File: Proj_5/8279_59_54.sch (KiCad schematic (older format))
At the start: 29 parts, among them SW10 Switch_SW_SPST, SW11 Switch_SW_SPST, SW12 Switch_SW_SPST, SW13 Switch_SW_SPST, SW14 Switch_SW_SPST, SW15 Switch_SW_SPST, SW16 Switch_SW_SPST, SW17 Switch_SW_SPST, SW18 Switch_SW_SPST, SW19 Switch_SW_SPST, SW2 Switch_SW_SPST, SW20 Switch_SW_SPST, SW21 Switch_SW_SPST, SW22 Switch_SW_SPST, SW23 Switch_SW_SPST, SW3 Switch_SW_SPST, SW4 Switch_SW_SPST, SW5 Switch_SW_SPST, SW6 Switch_SW_SPST, SW7 Switch_SW_SPST, SW8 Switch_SW_SPST, SW9 Switch_SW_SPST, U17 pkd8279, U18 74LS138

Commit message: Dont be wonky:
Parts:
- gave numbers to parts that had none: 5
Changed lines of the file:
@@
 P 6550 3000
 AR Path="/5EA98353/5EA655BD" Ref="C?"  Part="1"
-AR Path="/5EA993EC/5EA655BD" Ref="C?"  Part="1"
-F 0 "C?" V 6298 3000 50  0000 C CNN
+AR Path="/5EA993EC/5EA655BD" Ref="C11"  Part="1"
+F 0 "C11" V 6298 3000 50  0000 C CNN
 F 1 "0.1uF" V 6389 3000 50  0000 C CNN
 F 2 "" H 6588 2850 50  0001 C CNN
@@
 P 18350 4100
 AR Path="/5EA99146/5EA19E00" Ref="U?"  Part="1"
-AR Path="/5EA993EC/5EA19E00" Ref="U?"  Part="1"
-F 0 "U?" H 18350 5281 50  0000 C CNN
+AR Path="/5EA993EC/5EA19E00" Ref="U11"  Part="1"
+F 0 "U11" H 18350 5281 50  0000 C CNN
 F 1 "8254" H 18350 5190 50  0000 C CNN
 F 2 "Package_DIP:DIP-24_W15.24mm" H 18400 4350 50  0001 C CNN
@@
 AR Path="/5EA98353/5EA19E06" Ref="C?"  Part="1"
 AR Path="/5EA99146/5EA19E06" Ref="C?"  Part="1"
-AR Path="/5EA993EC/5EA19E06" Ref="C?"  Part="1"
-F 0 "C?" V 18448 2650 50  0000 C CNN
+AR Path="/5EA993EC/5EA19E06" Ref="C13"  Part="1"
+F 0 "C13" V 18448 2650 50  0000 C CNN
 F 1 "0.1uF" V 18539 2650 50  0000 C CNN
 F 2 "" H 18738 2500 50  0001 C CNN
@@
 P 13850 9850
 AR Path="/5EA99014/5EA1D8D0" Ref="U?"  Part="1"
-AR Path="/5EA993EC/5EA1D8D0" Ref="U?"  Part="1"
-F 0 "U?" H 13850 11131 50  0000 C CNN
+AR Path="/5EA993EC/5EA1D8D0" Ref="U10"  Part="1"
+F 0 "U10" H 13850 11131 50  0000 C CNN
 F 1 "8259" H 13850 11040 50  0000 C CNN
 F 2 "Package_DIP:DIP-28_W15.24mm" H 13850 9850 50  0001 C CIN
@@
 AR Path="/5EA98353/5EA1D8D6" Ref="C?"  Part="1"
 AR Path="/5EA99014/5EA1D8D6" Ref="C?"  Part="1"
-AR Path="/5EA993EC/5EA1D8D6" Ref="C?"  Part="1"
-F 0 "C?" V 13998 8500 50  0000 C CNN
+AR Path="/5EA993EC/5EA1D8D6" Ref="C12"  Part="1"
+F 0 "C12" V 13998 8500 50  0000 C CNN
 F 1 "0.1uF" V 14089 8500 50  0000 C CNN
 F 2 "" H 14288 8350 50  0001 C CNN

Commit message: Mostly finished 8279
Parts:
- removed C11: 0.1uF, symbol Device:C
- added C? (x4): 0.1uF, symbol Device:C
- added R?: R, symbol Device:R
- added SW? (x3): Switch_SW_SPST, symbol Proj_5-rescue:Switch_SW_SPST-Proj_5_Custom_LED
- added U? (x3): MAX6816, Package_TO_SOT_SMD:SOT-143, symbol Interface:MAX6816
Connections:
- net labels added: D0, D1, D2, D3, D4, D5, D6, D7, MAIN_CLK, NMI, RESET, ~RD, ~WR
- wire segments 110 -> 184
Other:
- note added: "Needs VCC Pins, Headers, Decoding"
- moved on the sheet: C12, C13

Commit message: Quick Edit to 79 Wires
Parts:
- R?: value R -> 1kOhm
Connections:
- wire segments 184 -> 187
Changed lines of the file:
@@
 	5550 5050 4700 5050
-Wire Wire Line
-	4700 550  14100 550
 Wire Wire Line
 	7150 8100 7700 8100
@@
 Wire Wire Line
 	10900 600  10900 1800
-Wire Wire Line
-	14100 600  14100 1850
 Wire Wire Line
 	4700 550  4700 5050
@@
 P 10550 8000
 F 0 "R?" H 10620 8046 50  0000 L CNN
-F 1 "R" H 10620 7955 50  0000 L CNN
+F 1 "1kOhm" H 10620 7955 50  0000 L CNN
 F 2 "" V 10480 8000 50  0001 C CNN
 F 3 "~" H 10550 8000 50  0001 C CNN
@@
 Text Notes 12550 7100 0    197  ~ 0
 Needs VCC Pins, Headers, Decoding
+Wire Wire Line
+	14100 600  14100 900
+Wire Wire Line
+	4700 550  13850 550
+Wire Wire Line
+	13850 550  13850 900
+Wire Wire Line
+	13850 900  14100 900
+Connection ~ 14100 900
+Wire Wire Line
+	14100 900  14100 1850
 $EndSCHEMATC

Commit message: Made the rest of the connections for the SRAM. Changed stuff on the main page
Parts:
- U10: symbol Interface:8259 -> Proj_5-rescue:8259-Interface
- U11: symbol Timer:8254 -> Proj_5-rescue:8254-Timer
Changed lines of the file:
@@
 	12050 3650 13050 3650
 $Comp
-L Timer:8254 U?
+L Proj_5-rescue:8254-Timer U?
 U 1 1 5EA19E00
 P 6550 7500
@@
 $EndComp
 $Comp
-L Interface:8259 U?
+L Proj_5-rescue:8259-Interface U?
 U 1 1 5EA1D8D0
 P 6450 2000
 AR Path="/5EA99014/5EA1D8D0" Ref="U?"  Part="1"
 AR Path="/5EA993EC/5EA1D8D0" Ref="U10"  Part="1"
+AR Path="/5EA1D8D0" Ref="U10"  Part="1"
 F 0 "U10" H 6450 3281 50  0000 C CNN
 F 1 "8259" H 6450 3190 50  0000 C CNN

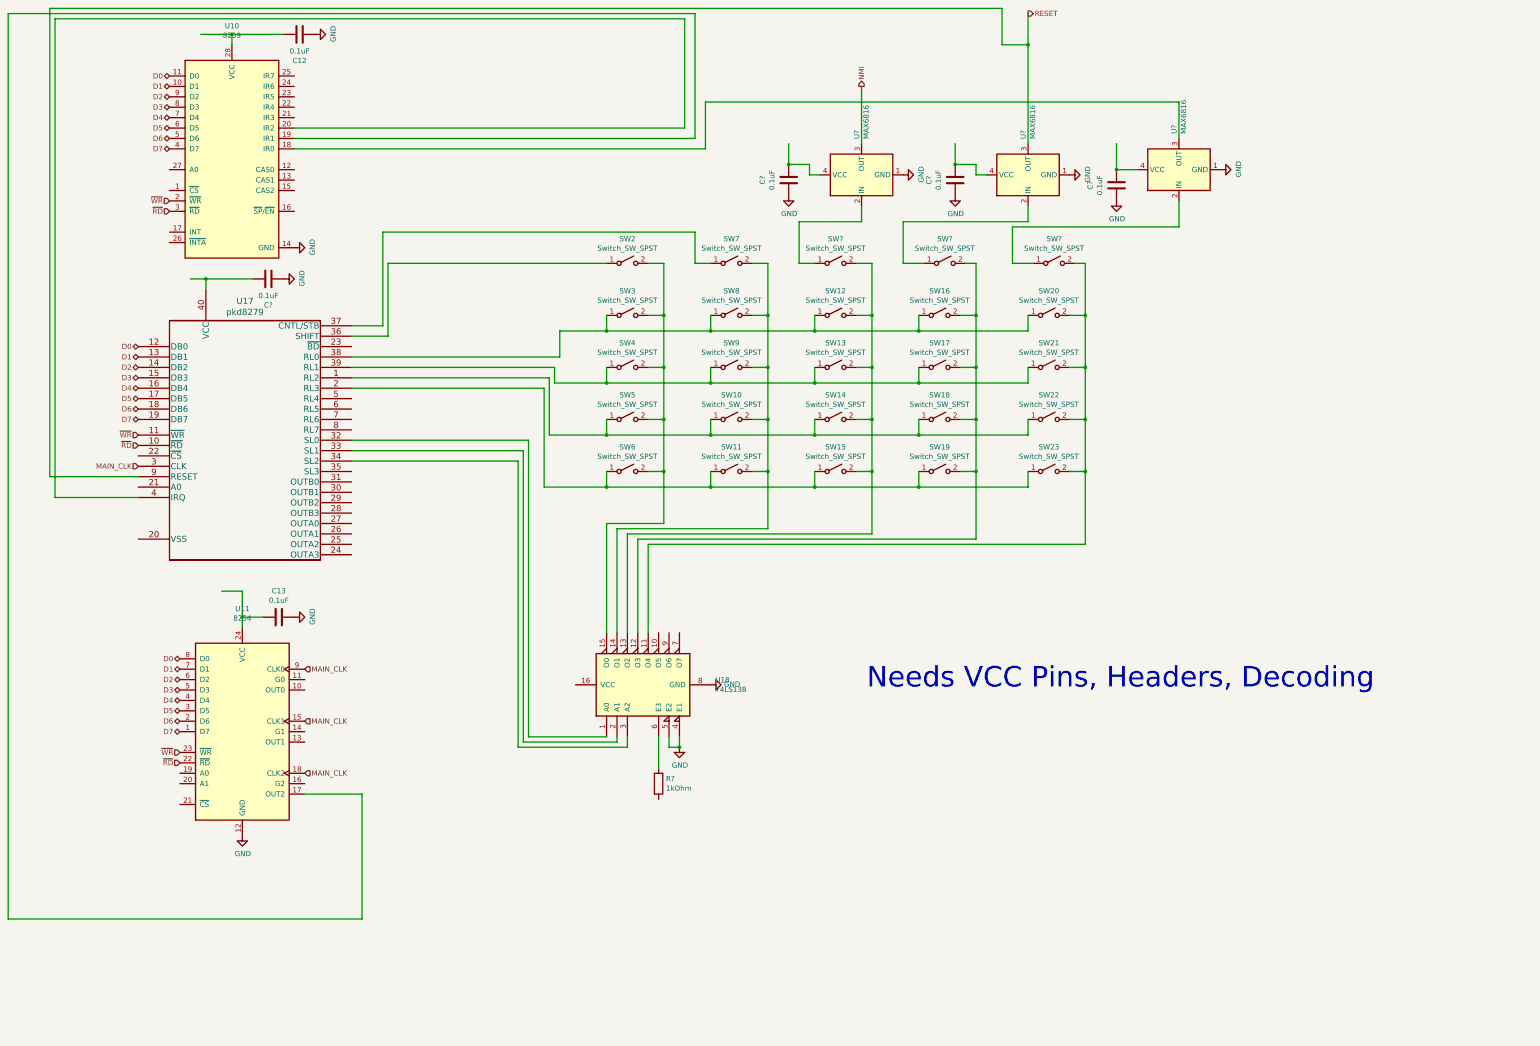
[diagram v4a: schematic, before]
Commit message: Changes to Top Level Connections
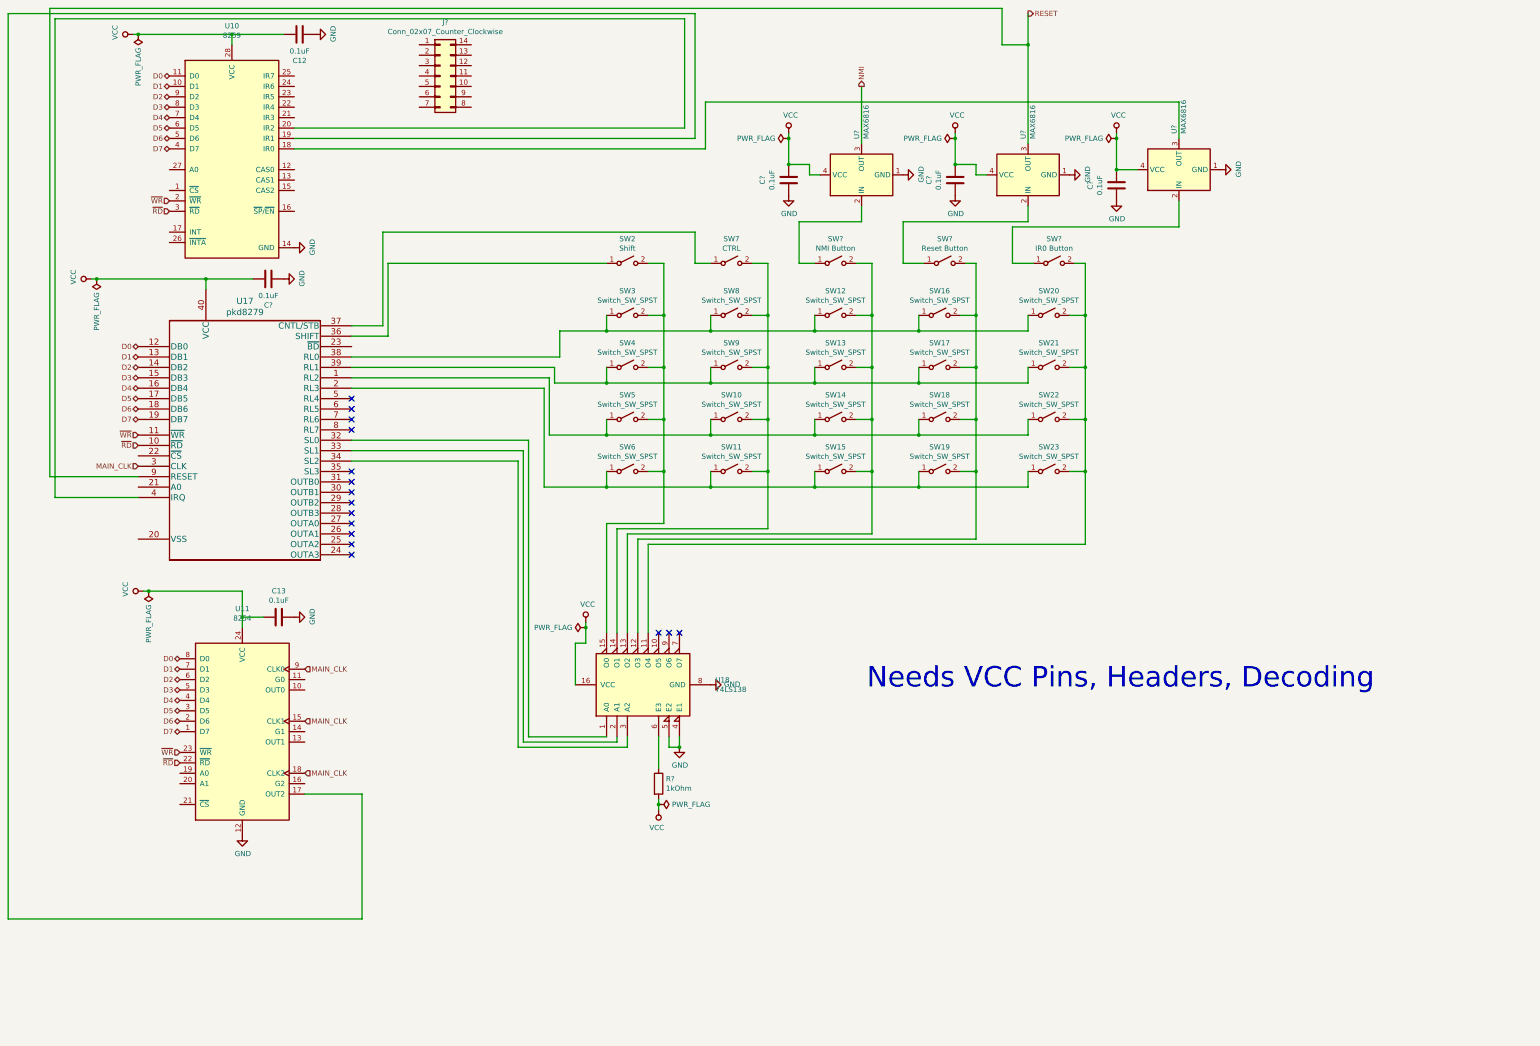
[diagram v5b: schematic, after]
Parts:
- added J?: Conn_02x07_Counter_Clockwise, symbol Connector_Generic:Conn_02x07_Counter_Clockwise
- SW2: value Switch_SW_SPST -> Shift
- SW7: value Switch_SW_SPST -> CTRL
- SW?: value Switch_SW_SPST -> NMI Button
- SW?: value Switch_SW_SPST -> Reset Button
- SW?: value Switch_SW_SPST -> IR0 Button
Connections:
- net labels added: VCC
- wire segments 187 -> 199
- no-connect marks 0 -> 16
